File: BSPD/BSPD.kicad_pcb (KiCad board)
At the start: 2 copper layers, 167.9 x 124.7 mm, 53 parts, among them J1 DT13-48PABCD-R015, K1 Latching Relay, Q2 STS6NF20V, Q3 STS6NF20V, U1 LM7805CT, U10 DK1A1B-12V, U11 NSL-32, U12 OP AMP, U14 ISO1050DUB, U15 LM7809_TO220, U2 OP AMP, U3 OP AMP, U4 NUCLEO-L432KC, U5 2x4 OR GATE, U6 LM555N, U7 NSL-32, U8 NAND, U9 AND GATE

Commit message: Moved default kicad models to folder and finished 3d models for board
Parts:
- R15, R6: value 374 -> 370
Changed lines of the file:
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@@
     (pad "8" smd roundrect (at 4.525 -3.81 180) (size 2.35 0.65) (layers "F.Cu" "F.Paste" "F.Mask") (roundrect_rratio 0.25)
       (net 2 "+5V") (pinfunction "VCC2") (pintype "power_in"))
-    (model "${KICAD6_3DMODEL_DIR}/Package_SO.3dshapes/SOP-8_6.62x9.15mm_P2.54mm.wrl"
+    (model "${FS_2_SCHEMATICS}/3D Models/DUB0008A.stp"
       (offset (xyz 0 0 0))
       (scale (xyz 1 1 1))
@@
     (pad "4" smd roundrect (at 2.932 -1.24 90) (size 2.5 0.6) (layers "F.Cu" "F.Paste" "F.Mask") (roundrect_rratio 0.25)
       (net 1 "+12V") (pinfunction "R") (pintype "passive") (thermal_bridge_angle 45))
+    (model "${FS_2_SCHEMATICS}/3D Models/4pin SO6.step"
+      (offset (xyz 0 0 0))
+      (scale (xyz 1 1 1))
+      (rotate (xyz 0 0 90))
+    )
   )
   (footprint "Capacitor_SMD:C_0805_2012Metric_Pad1.18x1.45mm_HandSolder" (layer "F.Cu")
@@
     (pad "6" thru_hole circle (at 5.08 -7.62) (size 1.524 1.524) (drill 0.762) (layers "*.Cu" "*.Mask")
       (net 50 "/SH_RESET") (pintype "passive"))
+    (model "${FS_2_SCHEMATICS}/3D Models/g6bk-1114p-us_12dc.stp"
+      (offset (xyz 1.3 -1.35 0))
+      (scale (xyz 1 1 1))
+      (rotate (xyz -90 0 90))
+    )
   )
   (footprint "Capacitor_SMD:C_0805_2012Metric_Pad1.18x1.45mm_HandSolder" (layer "F.Cu")
@@
     (pad "4" smd roundrect (at 2.932 -1.24 90) (size 2.5 0.6) (layers "F.Cu" "F.Paste" "F.Mask") (roundrect_rratio 0.25)
       (net 1 "+12V") (pinfunction "R") (pintype "passive") (thermal_bridge_angle 45))
+    (model "${FS_2_SCHEMATICS}/3D Models/4pin SO6.step"
+      (offset (xyz 0 0 0))
+      (scale (xyz 1 1 1))
+      (rotate (xyz 0 0 90))
+    )
   )
   (footprint "Diode_SMD:D_2010_5025Metric_Pad1.52x2.65mm_HandSolder" (layer "F.Cu")
@@
     (pad "8" thru_hole circle (at 10.16 0) (size 1.651 1.651) (drill 1.143) (layers "*.Cu" "*.Mask")
       (net 51 "Net-(D3-K)") (pinfunction "+") (pintype "power_in"))
+    (model "${FS_2_SCHEMATICS}/3D Models/RELAY_DK2A_PAN.step"
+      (offset (xyz 0 0 0))
+      (scale (xyz 1 1 1))
+      (rotate (xyz 0 0 0))
+    )
   )
   (footprint "Diode_SMD:D_2010_5025Metric_Pad1.52x2.65mm_HandSolder" (layer "F.Cu")
@@
         (effects (font (size 1 1) (thickness 0.15)))
     )
-    (fp_text value "374" (at 0 1.65) (layer "F.Fab")
+    (fp_text value "370" (at 0 1.65) (layer "F.Fab")
         (effects (font (size 1 1) (thickness 0.15)))
     )
@@
     (pad "8" smd rect (at 2.4638 -1.905) (size 1.9812 0.5334) (layers "F.Cu" "F.Paste" "F.Mask")
       (net 57 "/BMS Light Low Side") (pinfunction "D") (pintype "unspecified"))
+    (model "${FS_2_SCHEMATICS}/3D Models/SO_8.STEP"
+      (offset (xyz 0 0 0))
+      (scale (xyz 1 1 1))
+      (rotate (xyz 0 0 0))
+    )
   )
   (footprint "Capacitor_SMD:C_0805_2012Metric_Pad1.18x1.45mm_HandSolder" (layer "F.Cu")
@@
     (pad "8" smd rect (at 2.4638 -1.905) (size 1.9812 0.5334) (layers "F.Cu" "F.Paste" "F.Mask")
       (net 58 "/IMD Light Low Side") (pinfunction "D") (pintype "unspecified"))
+    (model "${FS_2_SCHEMATICS}/3D Models/SO_8.STEP"
+      (offset (xyz 0 0 0))
+      (scale (xyz 1 1 1))
+      (rotate (xyz 0 0 0))
+    )
   )
   (footprint "Resistor_SMD:R_0805_2012Metric_Pad1.20x1.40mm_HandSolder" (layer "F.Cu")
@@
         (effects (font (size 1 1) (thickness 0.15)))
     )
-    (fp_text value "374" (at 0 1.65 90) (layer "F.Fab")
+    (fp_text value "370" (at 0 1.65 90) (layer "F.Fab")
         (effects (font (size 1 1) (thickness 0.15)))
     )

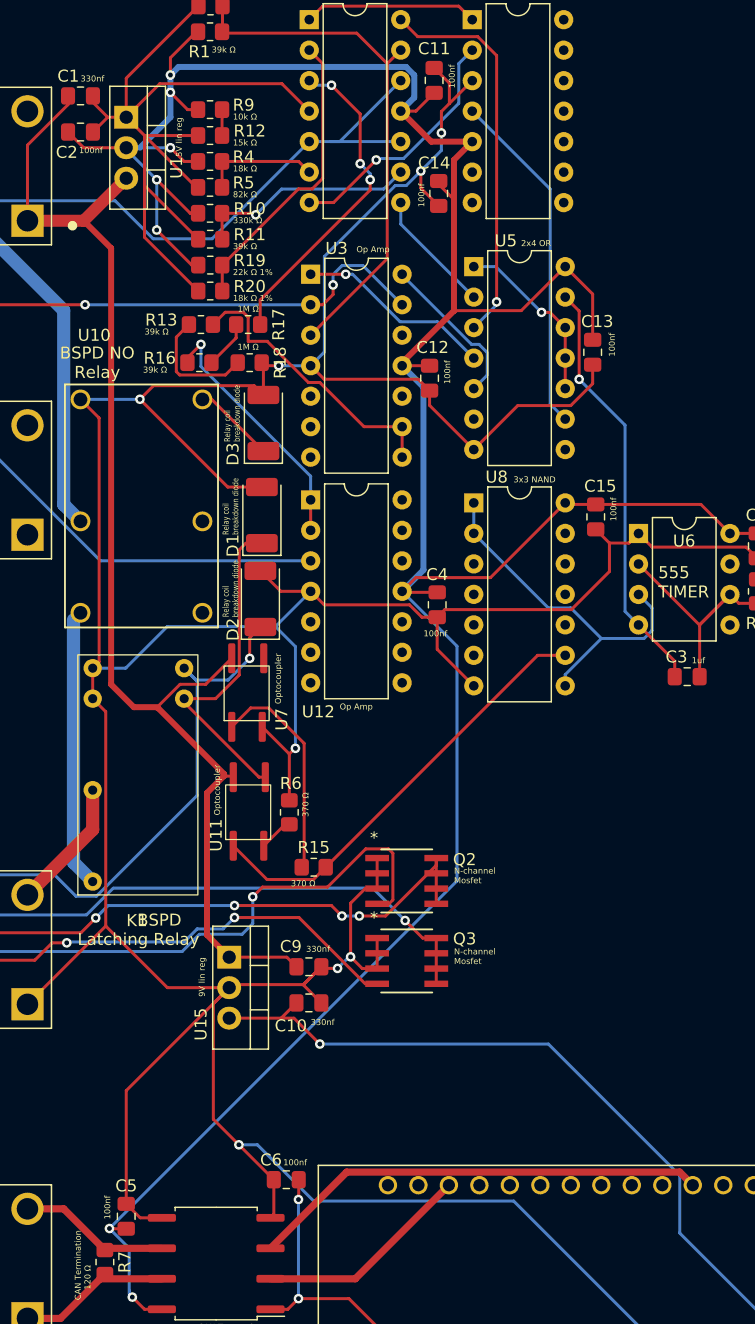
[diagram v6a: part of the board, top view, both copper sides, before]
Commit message: Made all traces non sharp angles on pads
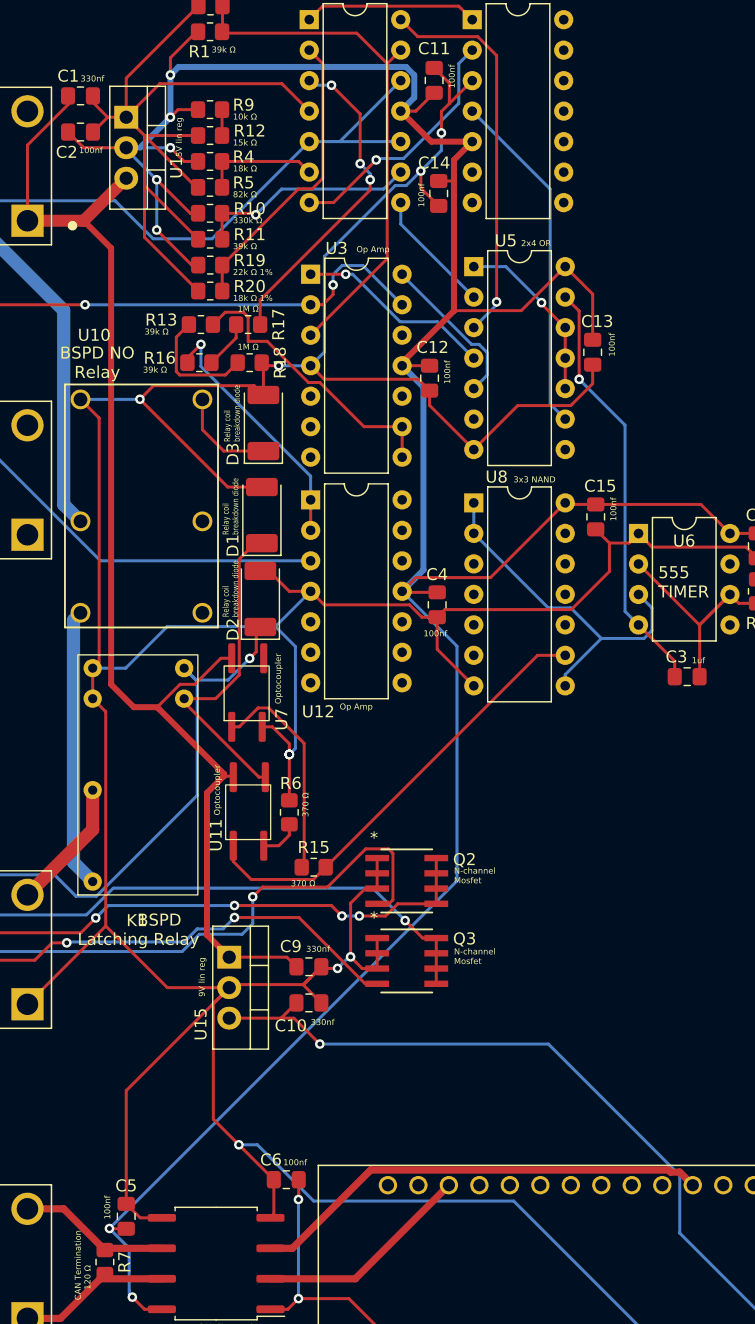
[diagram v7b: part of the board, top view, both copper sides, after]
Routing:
- net /BMS Light Low Side: track 51.7 -> 49.8 mm
- net Net-(D3-K): track 6.86 -> 8.34 mm
- net +5V: track 257.4 -> 256.3 mm
- net Net-(K1-Pad4): track 23.3 -> 22.5 mm
- net /BSPD Fault Post Timer: track 36.6 -> 37.3 mm
- net GND: track 469.1 -> 469.6 mm, vias 8 -> 10
- net Net-(U11-K): track 2.87 -> 3.40 mm

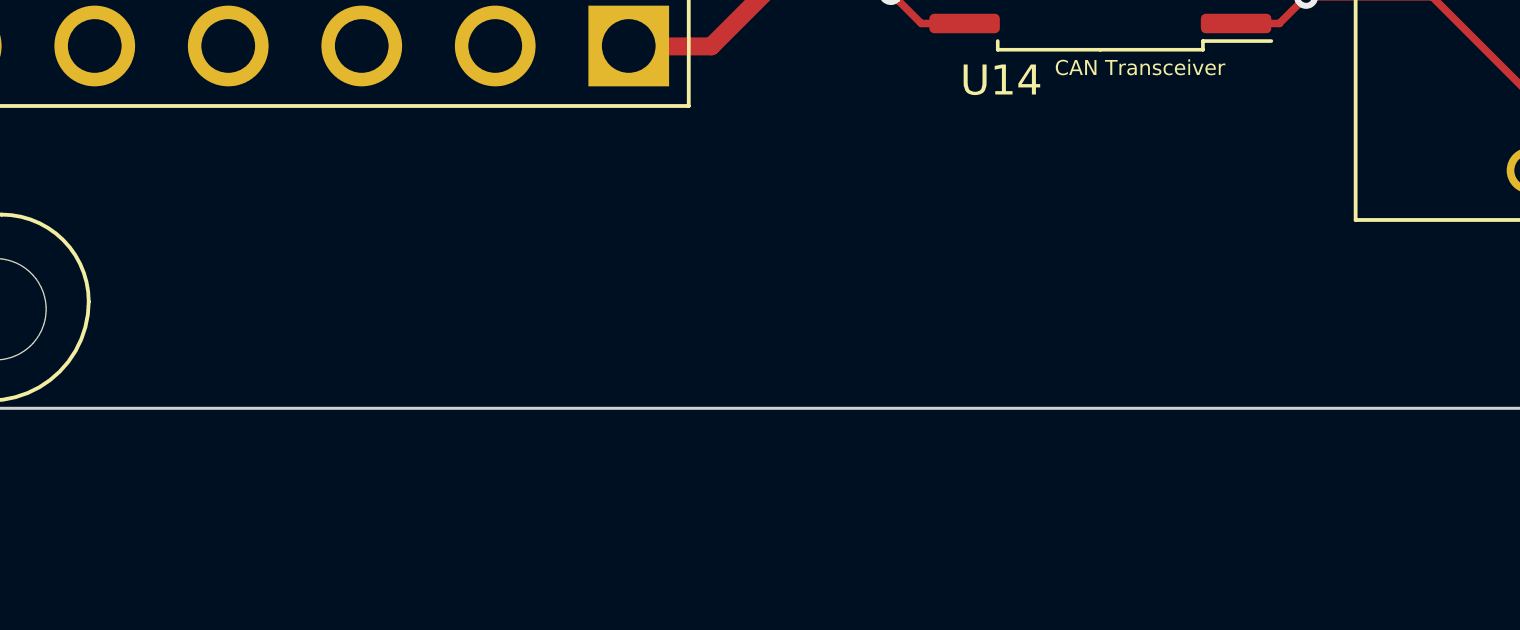
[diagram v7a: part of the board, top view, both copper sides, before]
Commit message: Added logo + updated board date
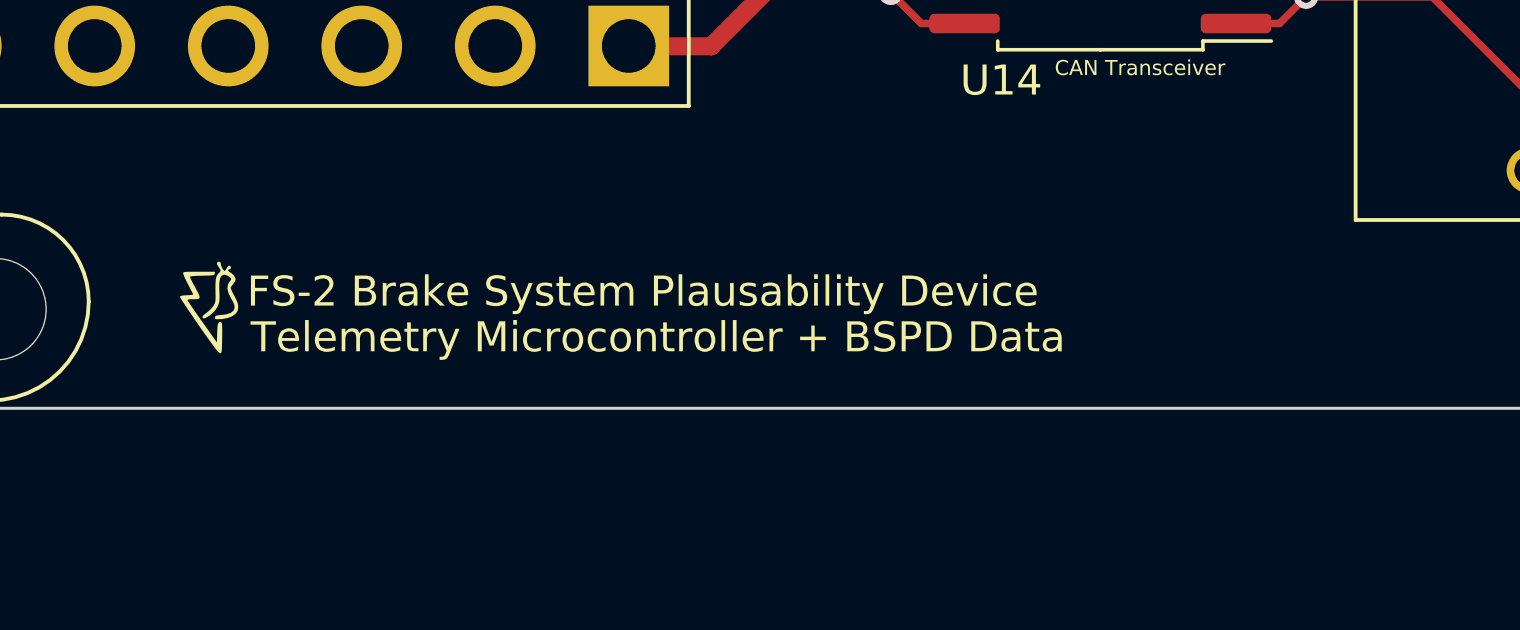
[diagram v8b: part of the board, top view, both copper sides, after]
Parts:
- added ?: , 1FS_2_Global_Footprint_Library:FORMULA SLUG, F.Cu at (43.3, 144.3)
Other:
- board text added: "FS-2 Brake System Plausability Device"
- board text added: "Telemetry Microcontroller + BSPD Data"
